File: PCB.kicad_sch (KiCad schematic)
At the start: 29 parts, among them J1 Conn_01x04, J2 Screw_Terminal_01x02, J3 Screw_Terminal_01x05, J4 Screw_Terminal_01x05, K1 G5LE-1A_DC3, K2 G5LE-1A_DC3, K3 G5LE-1, K4 G5LE-1, K6 G5LE-1, K7 G5LE-1A_DC3, Q1 DMN65D8L-7, Q2 DMN65D8L-7, Q3 DMN65D8L-7, SW2 SW_SPDT, SW3 Local DI2 (decspeed), SW4 local DI0 (onoff), SW5 Local DI1 (incspeed), U1 WeMos_D1_mini

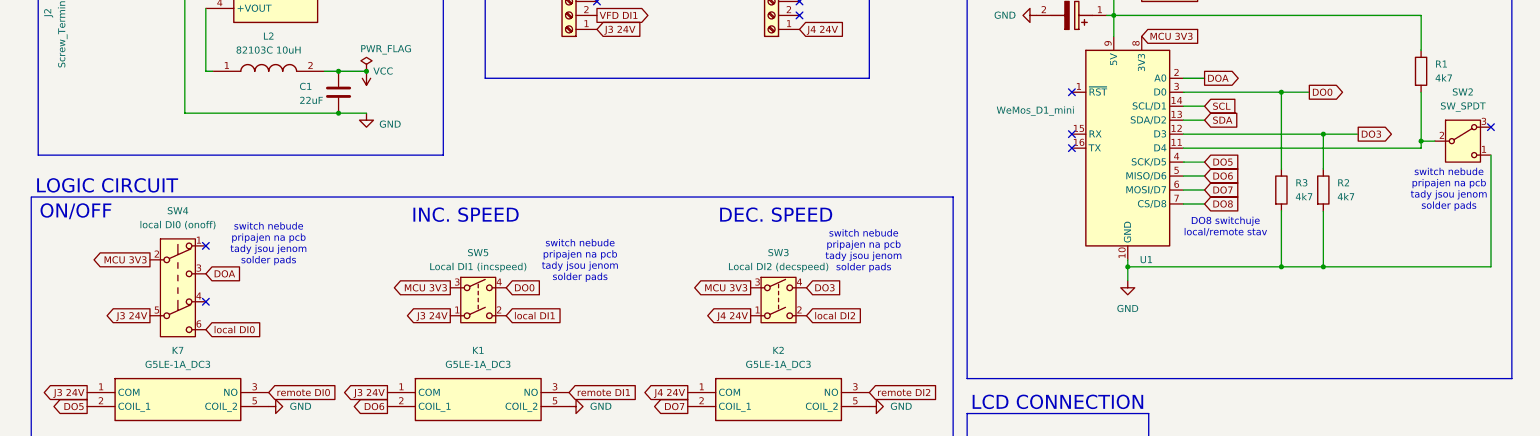
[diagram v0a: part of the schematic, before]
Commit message: remove the lots of vias so the layout is cleaner
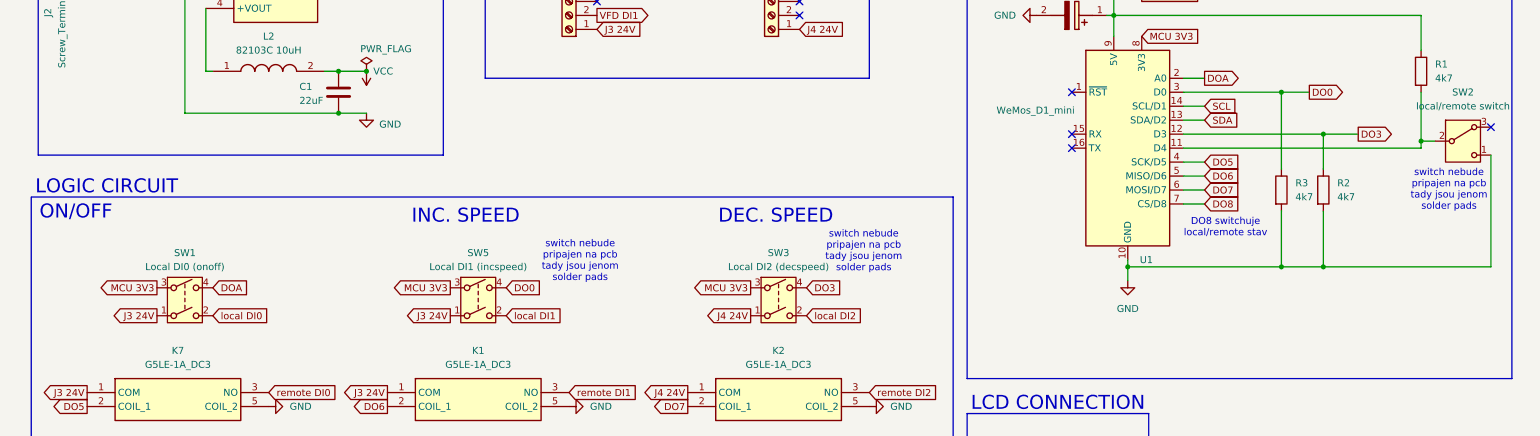
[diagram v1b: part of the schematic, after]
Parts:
- removed SW4: local DI0 (onoff), Connector_Wire:SolderWire-0.5sqmm_1x04_P4.8mm_D0.9mm_OD2.3mm_Relief, symbol Switch:SW_Push_DPDT
- added SW1: Local DI0 (onoff), Connector_Wire:SolderWire-0.5sqmm_1x04_P4.8mm_D0.9mm_OD2.3mm_Relief, symbol Switch:SW_DPST
- SW2: value SW_SPDT -> local/remote switch
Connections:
- net DOA: now also SW1.4
- net J3 24V: now also SW1.1
- net MCU 3V3: now also SW1.3
- net local DI0: now also SW1.2
- no-connect marks 11 -> 9
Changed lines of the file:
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@@
 	)
 	(no_connect
-		(at 44.45 87.63)
-	)
-	(no_connect
 		(at 152.4 27.94)
 	)
 	(no_connect
-		(at 44.45 77.47)
-	)
-	(no_connect
 		(at 201.93 57.15)
 	)
@@
 		)
 	)
-	(text "switch nebude\npripajen na pcb\ntady jsou jenom \nsolder pads"
-		(exclude_from_sim no)
-		(at 55.88 77.216 0)
-		(effects
-			(font
-				(size 1.27 1.27)
-			)
-		)
-	)
 	(text "devboard by mel brat max 450 mA a ma IO pin proud 12mA"
 		(exclude_from_sim no)
@@
 	(global_label "DOA"
 		(shape input)
-		(at 44.45 82.55 0)
+		(at 45.72 85.09 0)
 		(fields_autoplaced yes)
 		(effects
@@
 		)
 		(property "Intersheetrefs" "${INTERSHEET_REFS}"
-			(at 51.1243 82.55 0)
+			(at 52.3943 85.09 0)
 			(effects
 				(font
@@
 	(global_label "J3 24V"
 		(shape output)
-		(at 34.29 90.17 180)
+		(at 35.56 90.17 180)
 		(fields_autoplaced yes)
 		(effects
@@
 		)
 		(property "Intersheetrefs" "${INTERSHEET_REFS}"
-			(at 24.6525 90.17 0)
+			(at 25.9225 90.17 0)
 			(effects
 				(font
@@
 	(global_label "local DI0"
 		(shape input)
-		(at 44.45 92.71 0)
+		(at 45.72 90.17 0)
 		(fields_autoplaced yes)
 		(effects
@@
 		)
 		(property "Intersheetrefs" "${INTERSHEET_REFS}"
-			(at 56.2041 92.71 0)
+			(at 57.4741 90.17 0)
 			(effects
 				(font
@@
 	(global_label "MCU 3V3"
 		(shape output)
-		(at 34.29 80.01 180)
+		(at 35.56 85.09 180)
 		(fields_autoplaced yes)
 		(effects
@@
 		)
 		(property "Intersheetrefs" "${INTERSHEET_REFS}"
-			(at 22.7777 80.01 0)
+			(at 24.0477 85.09 0)
 			(effects
 				(font
@@
 	)
 	(symbol
+		(lib_id "Switch:SW_DPST")
+		(at 40.64 87.63 0)
+		(unit 1)
+		(exclude_from_sim no)
+		(in_bom yes)
+		(on_board yes)
+		(dnp no)
+		(fields_autoplaced yes)
+		(property "Reference" "SW1"
+			(at 40.64 78.74 0)
+			(effects
+				(font
+					(size 1.27 1.27)
+				)
+			)
+		)
+		(property "Value" "Local DI0 (onoff)"
+			(at 40.64 81.28 0)
+			(effects
+				(font
+					(size 1.27 1.27)
+				)
+			)
+		)
+		(property "Footprint" "Connector_Wire:SolderWire-0.5sqmm_1x04_P4.8mm_D0.9mm_OD2.3mm_Relief"
+			(at 40.64 87.63 0)
+			(effects
+				(font
+					(size 1.27 1.27)
+				)
+				(hide yes)
+			)
+		)
+		(property "Datasheet" "~"
+			(at 40.64 87.63 0)
+			(effects
+				(font
+					(size 1.27 1.27)
+				)
+				(hide yes)
+			)
+		)
+		(property "Description" "Double Pole Single Throw (DPST) Switch"
+			(at 40.64 87.63 0)
+			(effects
+				(font
+					(size 1.27 1.27)
+				)
+				(hide yes)
+			)
+		)
+		(pin "3"
+		)
+		(pin "1"
+		)
+		(pin "2"
+		)
+		(pin "4"
+		)
+		(instances
+			(project "PCB"
+				(path "/a03e0b08-fd2d-4304-b838-c1c22de42e47"
+					(reference "SW1")
+					(unit 1)
+				)
+			)
+		)
+	)
+	(symbol
 		(lib_id "Relay:G5LE-1")
 		(at 151.13 144.78 270)
@@
 			)
 		)
-		(property "Value" "SW_SPDT"
+		(property "Value" "local/remote switch"
 			(at 273.05 52.07 0)
 			(effects
@@
 					(unit 1)
 				)
-			)
-		)
-	)
-	(symbol
-		(lib_id "Switch:SW_Push_DPDT")
-		(at 39.37 85.09 0)
-		(unit 1)
-		(exclude_from_sim no)
-		(in_bom yes)
-		(on_board yes)
-		(dnp no)
-		(fields_autoplaced yes)
-		(property "Reference" "SW4"
-			(at 39.37 71.12 0)
-			(effects
-				(font
-					(size 1.27 1.27)
-				)
-			)
-		)
-		(property "Value" "local DI0 (onoff)"
-			(at 39.37 73.66 0)
-			(effects
-				(font
-					(size 1.27 1.27)
-				)
-			)
-		)
-		(property "Footprint" "Connector_Wire:SolderWire-0.5sqmm_1x04_P4.8mm_D0.9mm_OD2.3mm_Relief"
-			(at 39.37 80.01 0)
-			(effects
-				(font
-					(size 1.27 1.27)
-				)
-				(hide yes)
-			)
-		)
-		(property "Datasheet" "~"
-			(at 39.37 80.01 0)
-			(effects
-				(font
-					(size 1.27 1.27)
-				)
-				(hide yes)
-			)
-		)
-		(property "Description" "Momentary Switch, dual pole double throw"
-			(at 39.37 85.09 0)
-			(effects
-				(font
-					(size 1.27 1.27)
-				)
-				(hide yes)
-			)
-		)
-		(pin "5"
-		)
-		(pin "2"
-		)
-		(pin "1"
-		)
-		(pin "6"
-		)
-		(pin "3"
-		)
-		(pin "4"
-		)
-		(instances
-			(project ""
-				(path "/a03e0b08-fd2d-4304-b838-c1c22de42e47"
-					(reference "SW4")
-					(unit 1)
-				)

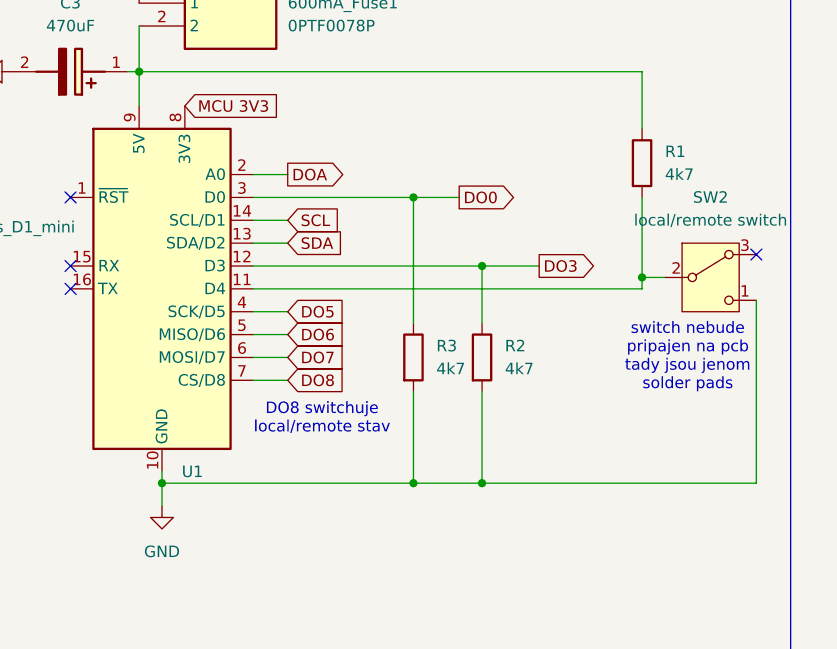
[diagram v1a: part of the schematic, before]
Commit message: widen tracks with larger current and fix the local/remote switch footprint
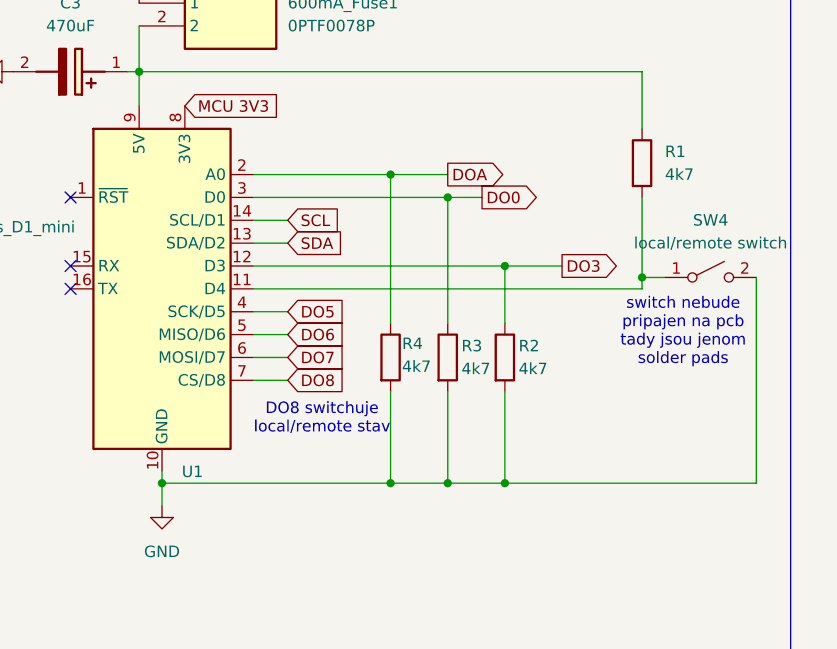
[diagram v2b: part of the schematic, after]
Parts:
- removed SW2: local/remote switch, Connector_Wire:SolderWire-0.5sqmm_1x02_P4.8mm_D0.9mm_OD2.3mm_Relief, symbol Switch:SW_Nidec_CAS-120A1
- added R4: 4k7, Resistor_SMD:R_0603_1608Metric, symbol Device:R
- added SW4: local/remote switch, Connector_Wire:SolderWire-0.5sqmm_1x02_P4.8mm_D0.9mm_OD2.3mm_Relief, symbol Switch:SW_SPST
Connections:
- net DOA: now also R4.1
- net GND: now also R4.2, SW4.2 (B)
- net at R1.2, U1.11 (D4): now also SW4.1 (A)
- no-connect marks 9 -> 8
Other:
- moved on the sheet: R2, R3

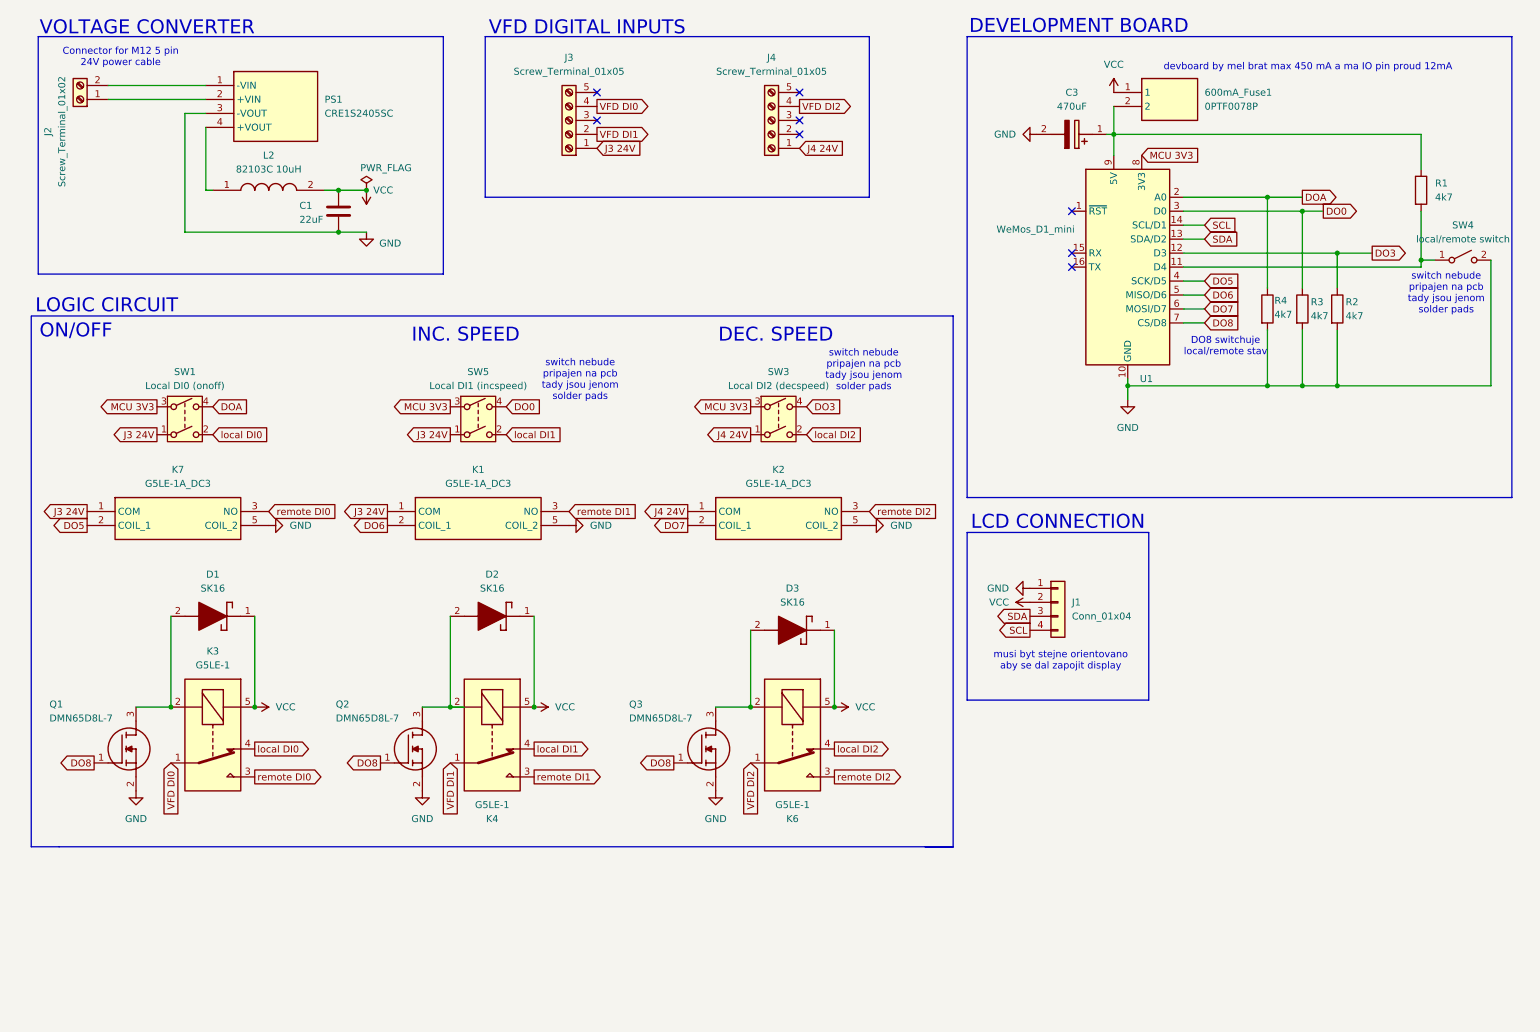
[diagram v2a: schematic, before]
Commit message: oprava schematu: zvoleni spravneho menice, pridani MOSFETu i k horni rade relay, move pojistky pred menicem a zvetseni hodnoty aby to utahla
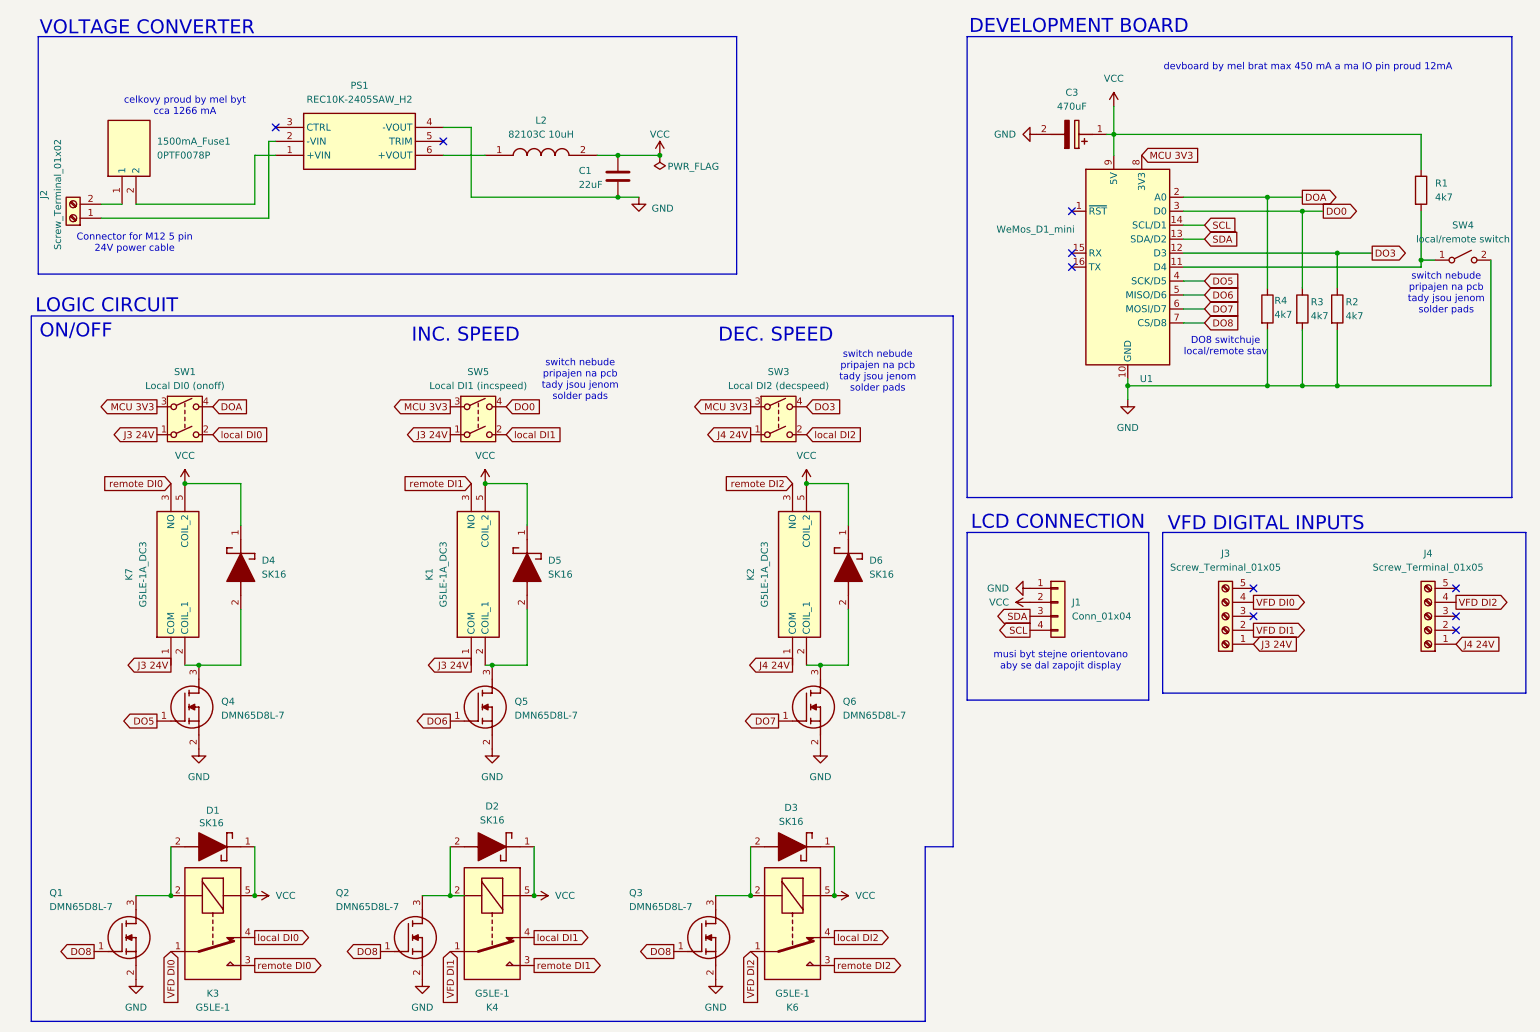
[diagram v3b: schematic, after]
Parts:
- removed PS1: CRE1S2405SC, Converter_DCDC:Converter_DCDC_Murata_CRE1xxxxxxSC_THT, symbol DCDC conv:CRE1S2405SC
- added D4, D5, D6: SK16, schottky:DIOM5027X250N, symbol schottky:SK16
- added PS1: REC10K-2405SAW_H2, dcdc converter:REC10K-AW, symbol DCDC conv:REC10K-2405SAW_H2
- added Q4, Q5, Q6: DMN65D8L-7, mosfet:SOT96P240X115-3N, symbol mosfet:DMN65D8L-7
- renumbered 600mA_Fuse1 to 1500mA_Fuse1
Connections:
- net DO5: now also Q4.1 (G); no longer K7.2 (COIL_1)
- net DO6: now also Q5.1 (G); no longer K1.2 (COIL_1)
- net DO7: now also Q6.1 (G); no longer K2.2 (COIL_1)
- net GND: now also PS1.4 (-VOUT), Q4.2 (S), Q5.2 (S), Q6.2 (S); no longer K1.5 (COIL_2), K2.5 (COIL_2), K7.5 (COIL_2)
- net VCC: now also C3.1 (+), K1.5 (COIL_2), K2.5 (COIL_2), K7.5 (COIL_2), R1.1, U1.9 (5V), D4.1 (K), D5.1 (K), D6.1 (K); no longer 1500mA_Fuse1.1
- net at L2.1: now also PS1.6 (+VOUT)
- net at J2.1 (Pin_1): now also PS1.2 (-VIN)
- net at J2.2 (Pin_2): now also 1500mA_Fuse1.1
- new net: D4.2 (A), K7.2 (COIL_1), Q4.3 (D)
- new net: 1500mA_Fuse1.2, PS1.1 (+VIN)
- new net: D6.2 (A), K2.2 (COIL_1), Q6.3 (D)
- new net: D5.2 (A), K1.2 (COIL_1), Q5.3 (D)
- no-connect marks 8 -> 10
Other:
- note added: "celkovy proud by mel byt cca 1266 mA"
- moved on the sheet: 1500mA_Fuse1, C1, D1, D2, D3, J2, J3, J4, K1, K2, K3, K4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
